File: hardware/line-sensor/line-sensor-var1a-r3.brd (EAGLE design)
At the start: 112 x 60 mm, 104 parts, among them IC1 GP2S60, IC10 GP2S60, IC11 GP2S60, IC12 GP2S60, IC13 GP2S60, IC14 GP2S60, IC15 GP2S60, IC16 GP2S60, IC17 GP2S60, IC18 GP2S60, IC19 GP2S60, IC2 GP2S60, IC20 GP2S60, IC21 GP2S60, IC22 GP2S60, IC23 GP2S60, IC24 GP2S60, IC25 GP2S60, IC26 GP2S60, IC27 GP2S60, IC28 STM32L151VE, IC3 GP2S60, IC32 LM5165YDRCR, IC4 GP2S60, IC5 GP2S60, IC6 GP2S60, IC7 GP2S60, IC8 GP2S60, IC9 GP2S60, J1 MOLEX-502382-06XX, J2 MOLEX-53261-0771, J3 MOLEX-502382-03XX, Y1 CRYSTALKYOCERA-CX5032GA

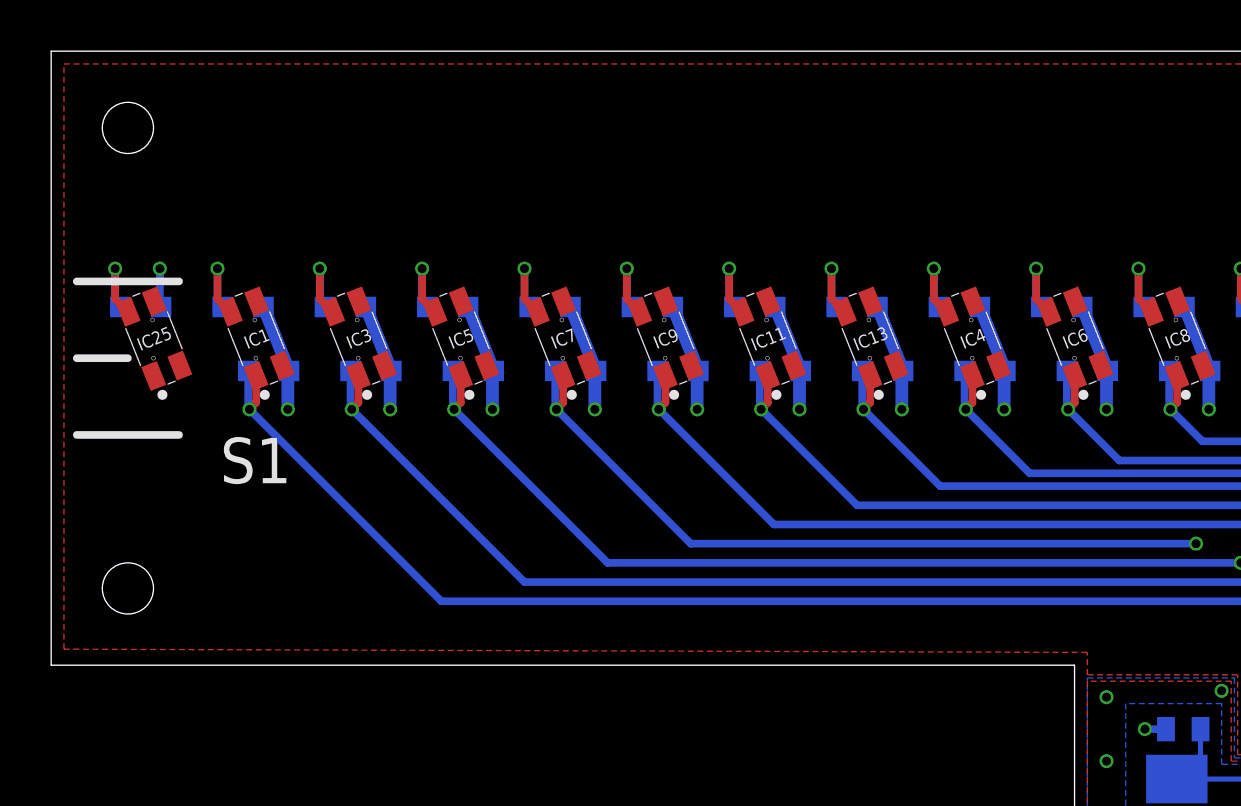
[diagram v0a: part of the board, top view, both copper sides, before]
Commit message: - removed old projects - fixed minor issues in line sensor pcb
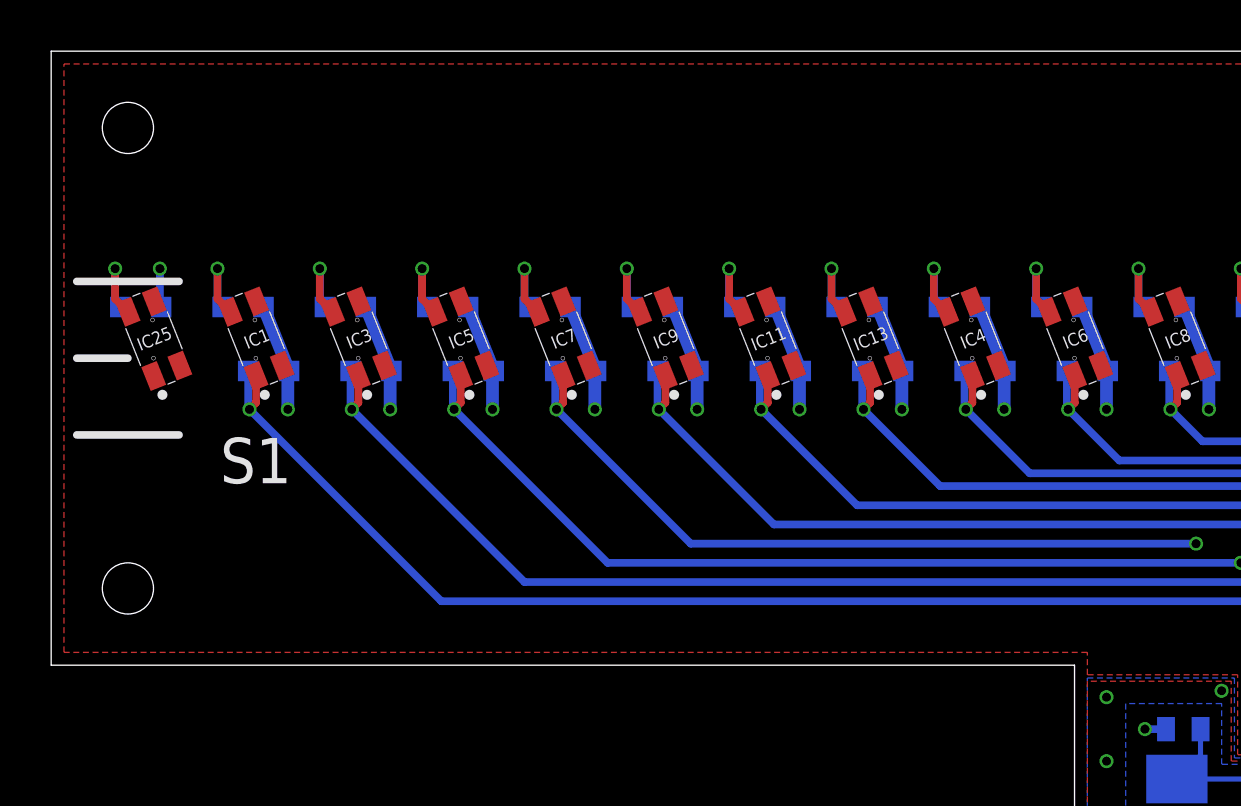
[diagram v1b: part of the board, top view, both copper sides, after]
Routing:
- net VDD: track 147.7 -> 146.9 mm
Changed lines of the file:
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@@
 <?xml version="1.0" encoding="utf-8"?>
 <!DOCTYPE eagle SYSTEM "eagle.dtd">
-<eagle version="9.5.1">
+<eagle version="9.5.2">
 <drawing>
 <settings>
@@
 <setting verticaltext="up"/>
 </settings>
-<grid distance="0.25" unitdist="mm" unit="mm" style="lines" multiple="1" display="yes" altdistance="5" altunitdist="mil" altunit="mil"/>
+<grid distance="0.1" unitdist="mm" unit="mm" style="lines" multiple="1" display="yes" altdistance="5" altunitdist="mil" altunit="mil"/>
 <layers>
 <layer number="1" name="Top" color="4" fill="1" visible="yes" active="yes"/>
@@
 <via x="88.25" y="56.75" extent="1-16" drill="0.35"/>
 <wire x1="65.3" y1="33" x2="65.9" y2="33.6" width="0.6" layer="2"/>
-<wire x1="65.3" y1="25.4" x2="65.9" y2="26" width="0.6" layer="2"/>
-<wire x1="65.9" y1="26" x2="65.9" y2="33.6" width="0.6" layer="2"/>
+<wire x1="65.3" y1="33" x2="65.3" y2="25.4" width="0.6" layer="2"/>
 <wire x1="32.3" y1="66" x2="33.3" y2="63.5" width="0.5" layer="16"/>
 <wire x1="36.3" y1="66" x2="37.3" y2="63.5" width="0.5" layer="16"/>
@@
 <vertex x="64.5" y="51.625"/>
 <vertex x="64.5" y="52.499609375"/>
-<vertex x="24.5" y="52.625"/>
+<vertex x="24.5" y="52.5"/>
 <vertex x="24.5" y="75.5"/>
 </polygon>
@@
 <via x="65.25" y="48.25" extent="1-16" drill="0.35"/>
 <via x="65.25" y="42.75" extent="1-16" drill="0.35"/>
+<wire x1="29.0306" y1="63.71214375" x2="28.02790625" y2="66.21905625" width="0" layer="19" extent="1-1"/>
 </signal>
 <signal name="STLINK_USART1_TX">
